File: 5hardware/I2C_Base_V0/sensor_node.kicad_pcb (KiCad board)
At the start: 2 copper layers, 70 parts, among them J1 USB_C_Receptacle_USB2.0, J2 PJ-320D-A, J3 Conn_02x06_Top_Bottom, J4 Conn_01x19_Socket, J5 Conn_01x19_Socket, J6 Conn_01x06_Socket, J7 Conn_01x04_Pin, J8 Conn_01x04_Pin, P1 S3B-PH-SM4-TB, P2 S4B-PH-SM4-TB, P3 S3B-PH-SM4-TB, Q2 Si2371EDS, Q3 Si2371EDS, SW2 SW_Push, SW3 SW_Push, U1 MCP1700x-330xxTO, U10 ESP-12F, U12 APDS-9960, U14 DS3231M, U3 CR2450, U4 CH32V003F4P6, U5 SHT31-DIS, U6 DS1307Z+, U7 XC6206PxxxMR, U8 TPL5110, U9 BH1750FVI-TR, Y1 Crystal, Y2 Crystal

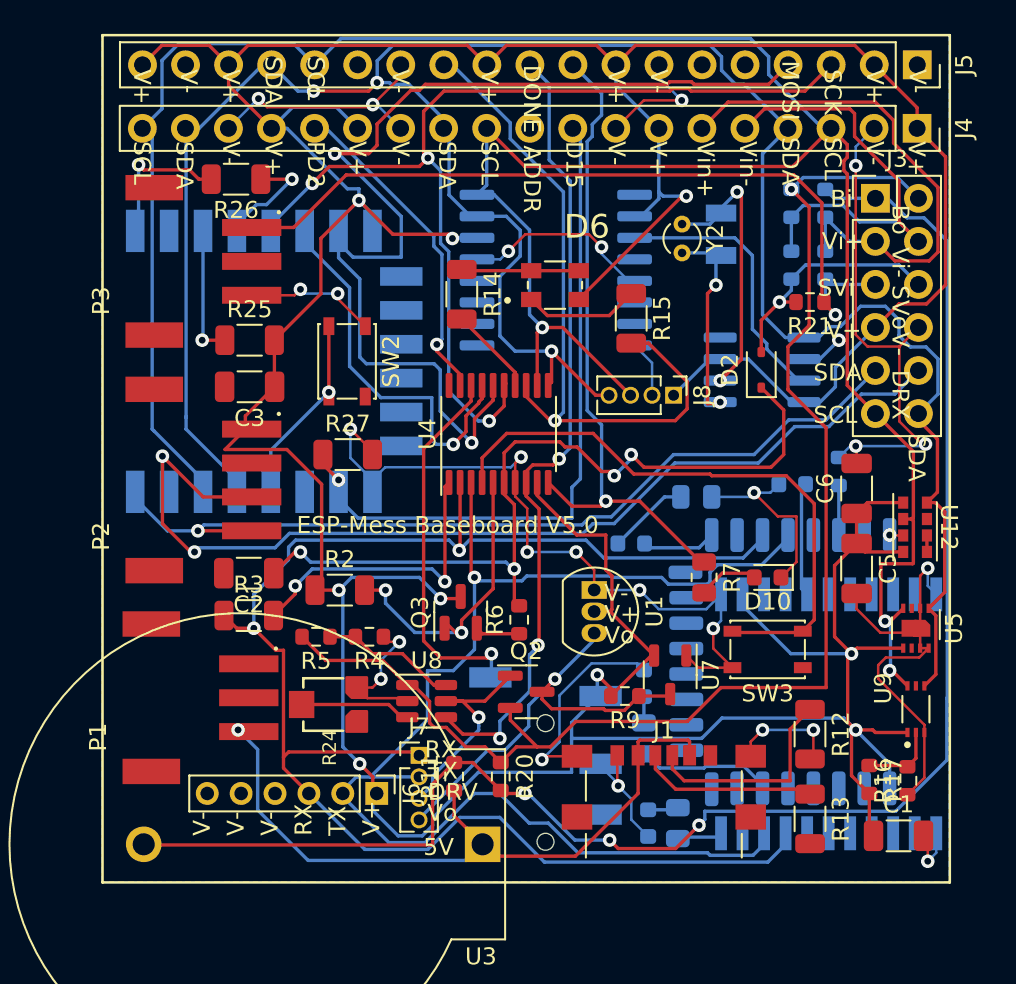
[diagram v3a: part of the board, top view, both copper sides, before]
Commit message: update schematic.
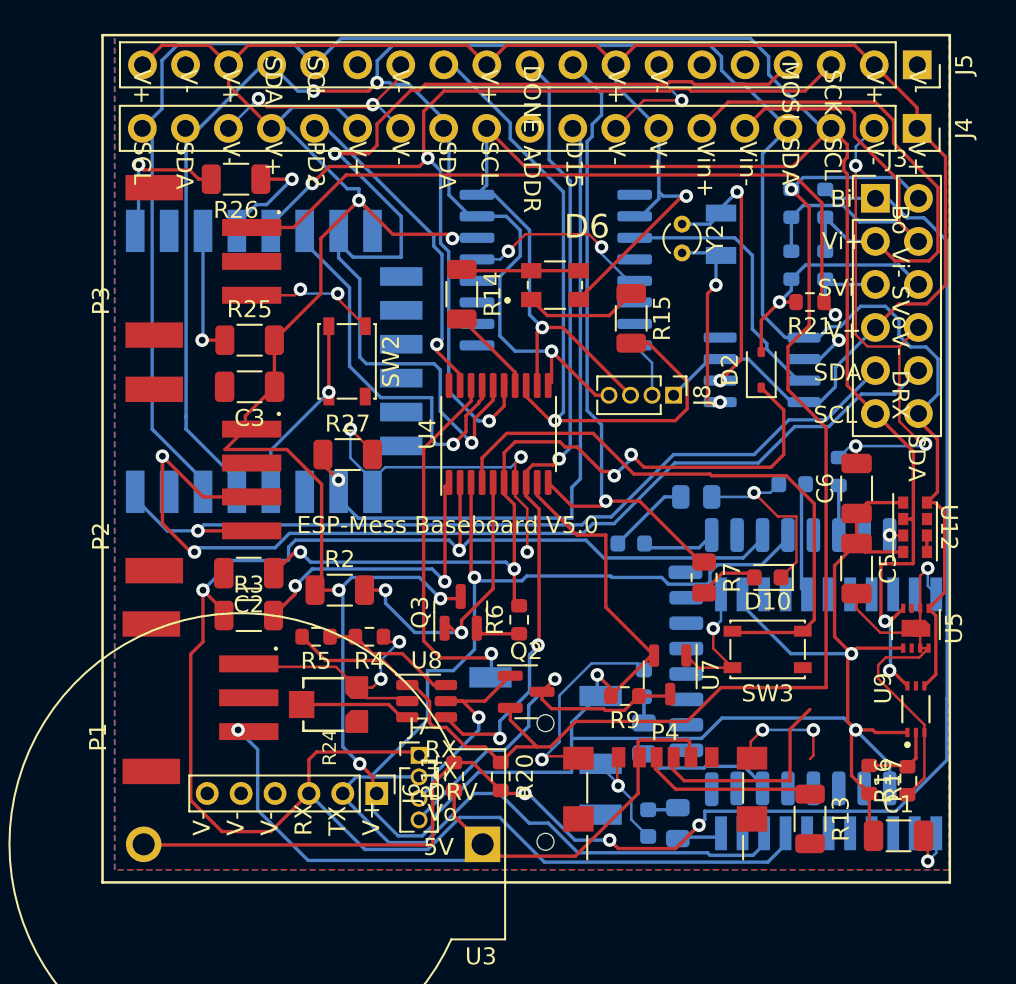
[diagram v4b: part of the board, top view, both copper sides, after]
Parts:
- removed J1: USB_C_Receptacle_USB2.0, Connector_USB:USB_C_Receptacle_GCT_USB4135-GF-A_6P_TopMnt_Horizontal
- removed R12: R, Resistor_SMD:R_1206_3216Metric
- removed U1: MCP1700x-330xxTO, Package_TO_SOT_THT:TO-92_Inline
- added P4: USB_C_Plug_USB2.0, Connector_USB:USB_C_Receptacle_GCT_USB4135-GF-A_6P_TopMnt_Horizontal, F.Cu at (133.3, 91.4)
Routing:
- net unconnected-(P4-VCONN-PadB5): track 0.00 -> 12.7 mm
- net Net-(J1-CC2): track 12.7 -> 0.00 mm
- net RX: track 93.6 -> 105.0 mm
- net GND: track 194.8 -> 187.9 mm, vias 26 -> 24
- net Vo: track 26.0 -> 22.0 mm
- net VCC: track 291.2 -> 290.2 mm

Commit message: update pcb.
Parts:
- removed P4: USB_C_Plug_USB2.0, Connector_USB:USB_C_Receptacle_GCT_USB4135-GF-A_6P_TopMnt_Horizontal
- removed R13: R, Resistor_SMD:R_1206_3216Metric
- moved R8 7.28 mm to (131.4, 80.0)
- moved D1 6.17 mm to (128.4, 79.0), turned to 0 degrees
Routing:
- net +5V: track 42.2 -> 25.3 mm
- net unconnected-(P4-VCONN-PadB5): track 12.7 -> 0.00 mm
- net Net-(P4-CC): track 10.8 -> 0.00 mm
- net Net-(U11-STAT): track 7.88 -> 16.1 mm
- net Bat-Vo: track 79.1 -> 85.5 mm
- net VCC: track 290.2 -> 292.6 mm, vias 9 -> 10
- net Net-(D1-A): track 1.64 -> 2.25 mm
- net GND: track 187.9 -> 187.8 mm, vias 24 -> 21

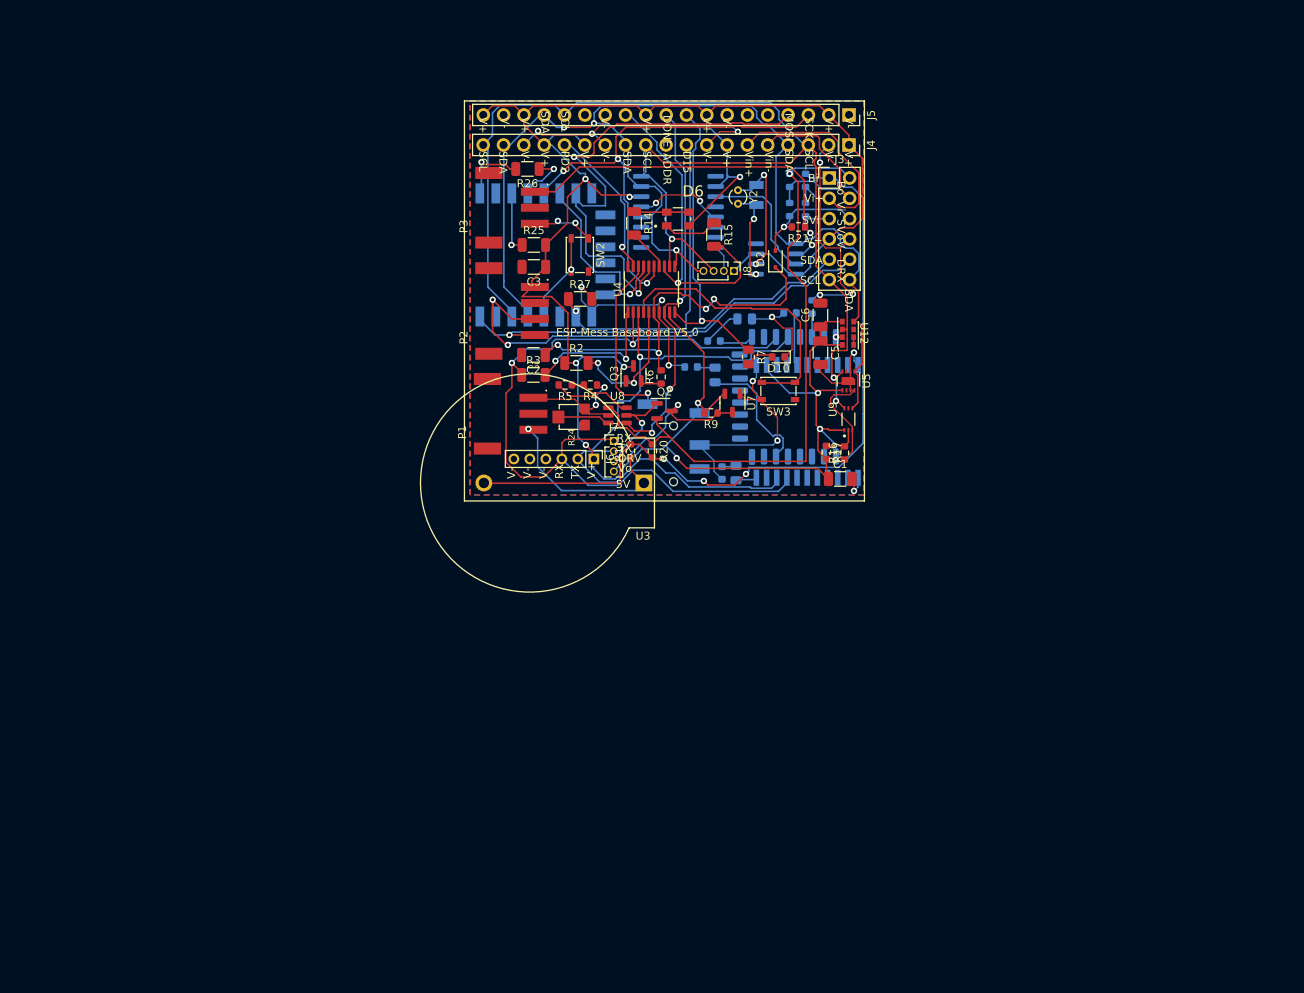
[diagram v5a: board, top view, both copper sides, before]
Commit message: panelized PCBs.
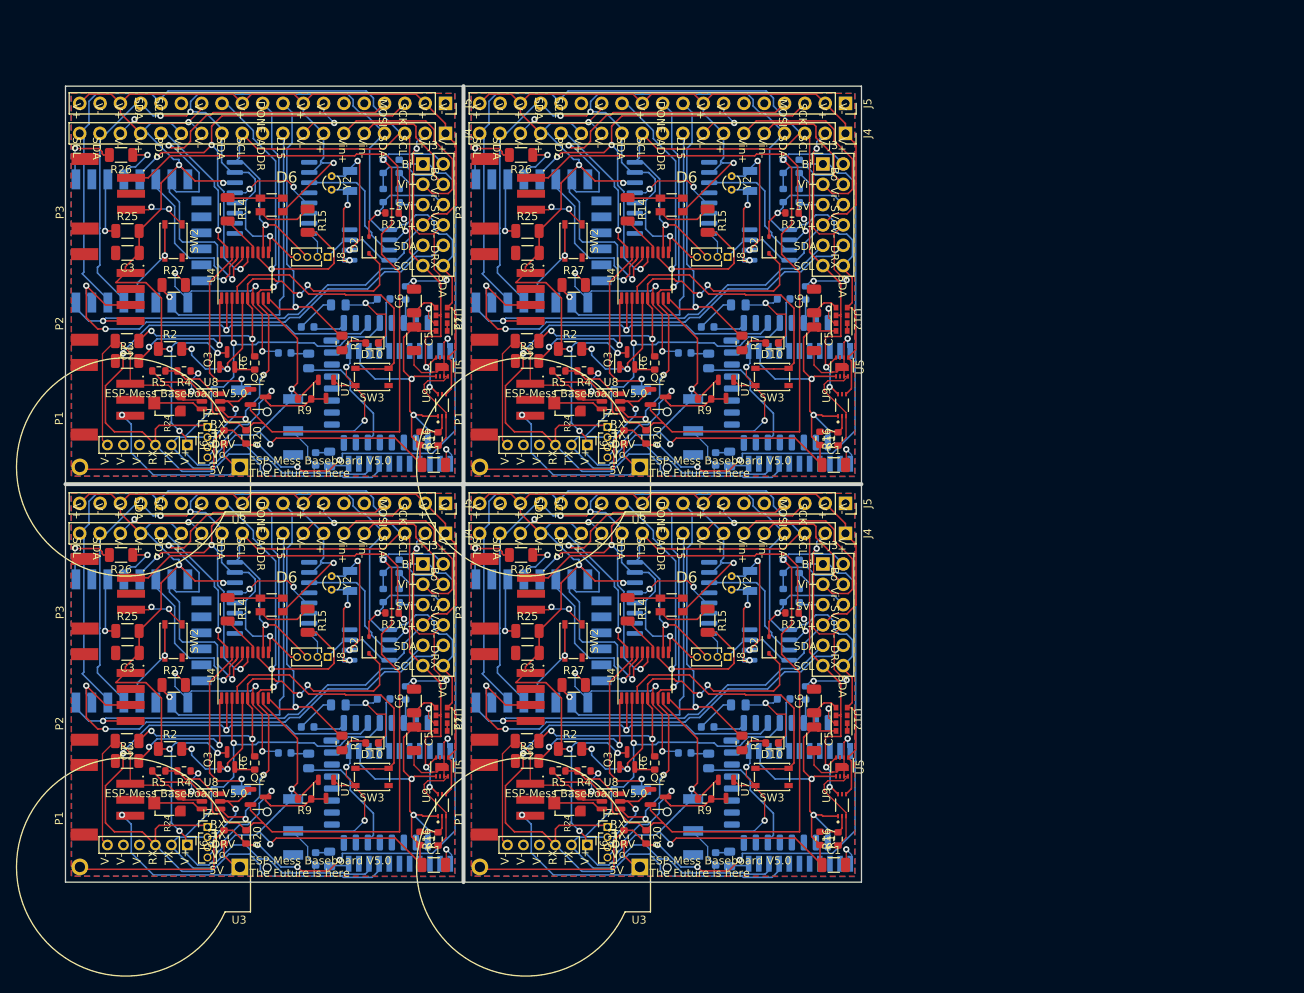
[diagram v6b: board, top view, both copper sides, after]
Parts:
- added C1: C, Capacitor_SMD:C_1206_3216Metric, F.Cu at (146.2, 141.2)
- added C1: C, Capacitor_SMD:C_1206_3216Metric, F.Cu at (96.2, 141.2)
- added C1: C, Capacitor_SMD:C_1206_3216Metric, F.Cu at (96.2, 91.2)
- added C2: C, Capacitor_SMD:C_1206_3216Metric, F.Cu at (57.9, 75.8)
- added C2: C, Capacitor_SMD:C_1206_3216Metric, F.Cu at (57.9, 125.8)
- added C2: C, Capacitor_SMD:C_1206_3216Metric, F.Cu at (107.9, 125.8)
- added C3: C, Capacitor_SMD:C_1206_3216Metric, F.Cu at (58.0, 64.8)
- added C3: C, Capacitor_SMD:C_1206_3216Metric, F.Cu at (58.0, 114.8)
- added C3: C, Capacitor_SMD:C_1206_3216Metric, F.Cu at (108.0, 114.8)
- added C5: C, Capacitor_SMD:C_1206_3216Metric, F.Cu at (143.8, 125.5)
- added C5: C, Capacitor_SMD:C_1206_3216Metric, F.Cu at (93.8, 75.5)
- added C5: C, Capacitor_SMD:C_1206_3216Metric, F.Cu at (93.8, 125.5)
- added C6: C, Capacitor_SMD:C_1206_3216Metric, F.Cu at (93.8, 120.8)
- added C6: C, Capacitor_SMD:C_1206_3216Metric, F.Cu at (93.8, 70.8)
- added C6: C, Capacitor_SMD:C_1206_3216Metric, F.Cu at (143.8, 120.8)
- added D1: LED, LED_SMD:LED_0603_1608Metric, B.Cu at (127.6, 127.2)
- added D1: LED, LED_SMD:LED_0603_1608Metric, B.Cu at (77.6, 77.2)
- added D1: LED, LED_SMD:LED_0603_1608Metric, B.Cu at (77.6, 127.2)
- added D10: LED, LED_SMD:LED_0603_1608Metric, F.Cu at (88.5, 126.0)
- added D10: LED, LED_SMD:LED_0603_1608Metric, F.Cu at (138.5, 126.0)
- added D10: LED, LED_SMD:LED_0603_1608Metric, F.Cu at (88.5, 76.0)
- added D2: D_Schottky, Diode_SMD:D_SOD-323, F.Cu at (88.1, 113.8)
- added D2: D_Schottky, Diode_SMD:D_SOD-323, F.Cu at (88.1, 63.8)
- added D2: D_Schottky, Diode_SMD:D_SOD-323, F.Cu at (138.1, 113.8)
- added D3: LED, LED_SMD:LED_0603_1608Metric, B.Cu at (130.5, 124.0)
- added D3: LED, LED_SMD:LED_0603_1608Metric, B.Cu at (80.5, 124.0)
- added D3: LED, LED_SMD:LED_0603_1608Metric, B.Cu at (80.5, 74.0)
- added D4: LED, LED_SMD:LED_0603_1608Metric, B.Cu at (140.0, 120.5)
- added D4: LED, LED_SMD:LED_0603_1608Metric, B.Cu at (90.0, 120.5)
- added D4: LED, LED_SMD:LED_0603_1608Metric, B.Cu at (90.0, 70.5)
- added D5: LED, LED_SMD:LED_0603_1608Metric, B.Cu at (81.5, 90.5)
- added D5: LED, LED_SMD:LED_0603_1608Metric, B.Cu at (131.5, 140.5)
- added D5: LED, LED_SMD:LED_0603_1608Metric, B.Cu at (81.5, 140.5)
- added D6: LL-R3528RGBC-008-B, R3528RGB:LED_LL-R3528RGBC-008-B, F.Cu at (76.0, 108.8)
- added D6: LL-R3528RGBC-008-B, R3528RGB:LED_LL-R3528RGBC-008-B, F.Cu at (126.0, 108.8)
- added D6: LL-R3528RGBC-008-B, R3528RGB:LED_LL-R3528RGBC-008-B, F.Cu at (76.0, 58.8)
- added J2: PJ-320D-A, A_SensorNode:PJ-320D, B.Cu at (75.4, 87.7)
- added J2: PJ-320D-A, A_SensorNode:PJ-320D, B.Cu at (125.4, 137.7)
- added J2: PJ-320D-A, A_SensorNode:PJ-320D, B.Cu at (75.4, 137.7)
- added J3: Conn_02x06_Top_Bottom, Connector_PinHeader_2.54mm:PinHeader_2x06_P2.54mm_Vertical, F.Cu at (94.9, 53.6)
- added J3: Conn_02x06_Top_Bottom, Connector_PinHeader_2.54mm:PinHeader_2x06_P2.54mm_Vertical, F.Cu at (94.9, 103.6)
- added J3: Conn_02x06_Top_Bottom, Connector_PinHeader_2.54mm:PinHeader_2x06_P2.54mm_Vertical, F.Cu at (144.9, 103.6)
- added J4: Conn_01x19_Socket, Connector_PinSocket_2.54mm:PinSocket_1x19_P2.54mm_Vertical, F.Cu at (97.7, 99.8)
- added J4: Conn_01x19_Socket, Connector_PinSocket_2.54mm:PinSocket_1x19_P2.54mm_Vertical, F.Cu at (97.7, 49.8)
- added J4: Conn_01x19_Socket, Connector_PinSocket_2.54mm:PinSocket_1x19_P2.54mm_Vertical, F.Cu at (147.7, 99.8)
- added J5: Conn_01x19_Socket, Connector_PinSocket_2.54mm:PinSocket_1x19_P2.54mm_Vertical, F.Cu at (97.7, 46.0)
- added J5: Conn_01x19_Socket, Connector_PinSocket_2.54mm:PinSocket_1x19_P2.54mm_Vertical, F.Cu at (147.7, 96.0)
- added J5: Conn_01x19_Socket, Connector_PinSocket_2.54mm:PinSocket_1x19_P2.54mm_Vertical, F.Cu at (97.7, 96.0)
- added J6: Conn_01x06_Socket, Connector_PinHeader_2.00mm:PinHeader_1x06_P2.00mm_Vertical, F.Cu at (65.5, 138.8)
- added J6: Conn_01x06_Socket, Connector_PinHeader_2.00mm:PinHeader_1x06_P2.00mm_Vertical, F.Cu at (65.5, 88.8)
- added J6: Conn_01x06_Socket, Connector_PinHeader_2.00mm:PinHeader_1x06_P2.00mm_Vertical, F.Cu at (115.5, 138.8)
- added J7: Conn_01x04_Pin, Connector_PinHeader_1.27mm:PinHeader_1x04_P1.27mm_Vertical, F.Cu at (68.0, 136.5)
- added J7: Conn_01x04_Pin, Connector_PinHeader_1.27mm:PinHeader_1x04_P1.27mm_Vertical, F.Cu at (68.0, 86.5)
- added J7: Conn_01x04_Pin, Connector_PinHeader_1.27mm:PinHeader_1x04_P1.27mm_Vertical, F.Cu at (118.0, 136.5)
- added J8: Conn_01x04_Pin, Connector_PinHeader_1.27mm:PinHeader_1x04_P1.27mm_Vertical, F.Cu at (83.0, 115.2)
- added J8: Conn_01x04_Pin, Connector_PinHeader_1.27mm:PinHeader_1x04_P1.27mm_Vertical, F.Cu at (83.0, 65.2)
- added J8: Conn_01x04_Pin, Connector_PinHeader_1.27mm:PinHeader_1x04_P1.27mm_Vertical, F.Cu at (133.0, 115.2)
- added P1: S3B-PH-SM4-TB, S3B-PH:JST_S3B-PH-SM4-TB, F.Cu at (58.3, 133.1)
- added P1: S3B-PH-SM4-TB, S3B-PH:JST_S3B-PH-SM4-TB, F.Cu at (108.3, 133.1)
- added P1: S3B-PH-SM4-TB, S3B-PH:JST_S3B-PH-SM4-TB, F.Cu at (58.3, 83.1)
- added P2: S4B-PH-SM4-TB, S4B-PH:JST_S4B-PH-SM4-TB, F.Cu at (58.4, 70.2)
- added P2: S4B-PH-SM4-TB, S4B-PH:JST_S4B-PH-SM4-TB, F.Cu at (108.3, 120.2)
- added P2: S4B-PH-SM4-TB, S4B-PH:JST_S4B-PH-SM4-TB, F.Cu at (58.4, 120.2)
- added P3: S3B-PH-SM4-TB, S3B-PH:JST_S3B-PH-SM4-TB, F.Cu at (108.4, 107.3)
- added P3: S3B-PH-SM4-TB, S3B-PH:JST_S3B-PH-SM4-TB, F.Cu at (58.4, 57.4)
- added P3: S3B-PH-SM4-TB, S3B-PH:JST_S3B-PH-SM4-TB, F.Cu at (58.4, 107.3)
- added Q2: Si2371EDS, Package_TO_SOT_SMD:SOT-23, F.Cu at (74.3, 132.8)
- added Q2: Si2371EDS, Package_TO_SOT_SMD:SOT-23, F.Cu at (124.3, 132.8)
- added Q2: Si2371EDS, Package_TO_SOT_SMD:SOT-23, F.Cu at (74.3, 82.8)
- added Q3: Si2371EDS, Package_TO_SOT_SMD:SOT-23, F.Cu at (70.4, 128.1)
- added Q3: Si2371EDS, Package_TO_SOT_SMD:SOT-23, F.Cu at (70.4, 78.1)
- added Q3: Si2371EDS, Package_TO_SOT_SMD:SOT-23, F.Cu at (120.4, 128.1)
- added R1: R, Resistor_SMD:R_0603_1608Metric, B.Cu at (142.7, 119.8)
- added R1: R, Resistor_SMD:R_0603_1608Metric, B.Cu at (92.7, 119.8)
- added R1: R, Resistor_SMD:R_0603_1608Metric, B.Cu at (92.7, 69.8)
- added R10: R, Resistor_SMD:R_0805_2012Metric, B.Cu at (133.2, 140.5)
- added R10: R, Resistor_SMD:R_0805_2012Metric, B.Cu at (83.2, 90.5)
- added R10: R, Resistor_SMD:R_0805_2012Metric, B.Cu at (83.2, 140.5)
- added R11: R, Resistor_SMD:R_0603_1608Metric, F.Cu at (70.0, 87.8)
- added R11: R, Resistor_SMD:R_0603_1608Metric, F.Cu at (120.0, 137.8)
- added R11: R, Resistor_SMD:R_0603_1608Metric, F.Cu at (70.0, 137.8)
- added R14: R, Resistor_SMD:R_1206_3216Metric, F.Cu at (70.5, 59.3)
- added R14: R, Resistor_SMD:R_1206_3216Metric, F.Cu at (70.5, 109.3)
- added R14: R, Resistor_SMD:R_1206_3216Metric, F.Cu at (120.5, 109.3)
- added R15: R, Resistor_SMD:R_1206_3216Metric, F.Cu at (80.5, 60.7)
- added R15: R, Resistor_SMD:R_1206_3216Metric, F.Cu at (80.5, 110.7)
- added R15: R, Resistor_SMD:R_1206_3216Metric, F.Cu at (130.5, 110.7)
- added R16: R, Resistor_SMD:R_0603_1608Metric, F.Cu at (96.8, 138.0)
- added R16: R, Resistor_SMD:R_0603_1608Metric, F.Cu at (96.8, 88.0)
- added R16: R, Resistor_SMD:R_0603_1608Metric, F.Cu at (146.8, 138.0)
- added R17: R, Resistor_SMD:R_0603_1608Metric, F.Cu at (144.5, 137.9)
- added R17: R, Resistor_SMD:R_0603_1608Metric, F.Cu at (94.5, 87.9)
- added R17: R, Resistor_SMD:R_0603_1608Metric, F.Cu at (94.5, 137.9)
- added R18: R, Resistor_SMD:R_0603_1608Metric, B.Cu at (91.9, 103.9)
- added R18: R, Resistor_SMD:R_0603_1608Metric, B.Cu at (91.9, 53.9)
- added R18: R, Resistor_SMD:R_0603_1608Metric, B.Cu at (141.9, 103.9)
- added R19: R, Resistor_SMD:R_0603_1608Metric, B.Cu at (139.9, 103.9)
- added R19: R, Resistor_SMD:R_0603_1608Metric, B.Cu at (89.9, 53.9)
- added R19: R, Resistor_SMD:R_0603_1608Metric, B.Cu at (89.9, 103.9)
- added R2: R, Resistor_SMD:R_1206_3216Metric, F.Cu at (113.3, 126.8)
- added R2: R, Resistor_SMD:R_1206_3216Metric, F.Cu at (63.3, 76.8)
- added R2: R, Resistor_SMD:R_1206_3216Metric, F.Cu at (63.3, 126.8)
- added R20: R, Resistor_SMD:R_0603_1608Metric, F.Cu at (72.8, 87.8)
- added R20: R, Resistor_SMD:R_0603_1608Metric, F.Cu at (72.8, 137.8)
- added R20: R, Resistor_SMD:R_0603_1608Metric, F.Cu at (122.8, 137.8)
- added R21: R, Resistor_SMD:R_0603_1608Metric, F.Cu at (141.0, 109.8)
- added R21: R, Resistor_SMD:R_0603_1608Metric, F.Cu at (91.0, 59.8)
- added R21: R, Resistor_SMD:R_0603_1608Metric, F.Cu at (91.0, 109.8)
- added R22: R, Resistor_SMD:R_0603_1608Metric, B.Cu at (91.9, 107.6)
- added R22: R, Resistor_SMD:R_0603_1608Metric, B.Cu at (141.9, 107.6)
- added R22: R, Resistor_SMD:R_0603_1608Metric, B.Cu at (91.9, 57.6)
- added R23: R, Resistor_SMD:R_0603_1608Metric, B.Cu at (89.9, 107.6)
- added R23: R, Resistor_SMD:R_0603_1608Metric, B.Cu at (139.9, 107.6)
- added R23: R, Resistor_SMD:R_0603_1608Metric, B.Cu at (89.9, 57.6)
- added R24: EVM3ESX50B12, EVM3ES:EMV3ESX50B12, F.Cu at (113.0, 133.5)
- added R24: EVM3ESX50B12, EVM3ES:EMV3ESX50B12, F.Cu at (63.0, 133.5)
- added R24: EVM3ESX50B12, EVM3ES:EMV3ESX50B12, F.Cu at (63.0, 83.5)
- added R25: R, Resistor_SMD:R_1206_3216Metric, F.Cu at (108.0, 112.0)
- added R25: R, Resistor_SMD:R_1206_3216Metric, F.Cu at (58.0, 62.0)
- added R25: R, Resistor_SMD:R_1206_3216Metric, F.Cu at (58.0, 112.0)
- added R26: R, Resistor_SMD:R_1206_3216Metric, F.Cu at (57.1, 52.5)
- added R26: R, Resistor_SMD:R_1206_3216Metric, F.Cu at (57.1, 102.5)
- added R26: R, Resistor_SMD:R_1206_3216Metric, F.Cu at (107.1, 102.5)
- added R27: R, Resistor_SMD:R_1206_3216Metric, F.Cu at (63.7, 118.8)
- added R27: R, Resistor_SMD:R_1206_3216Metric, F.Cu at (63.7, 68.8)
- added R27: R, Resistor_SMD:R_1206_3216Metric, F.Cu at (113.7, 118.8)
- added R28: R, Resistor_SMD:R_0805_2012Metric, B.Cu at (134.3, 121.2)
- added R28: R, Resistor_SMD:R_0805_2012Metric, B.Cu at (84.3, 71.2)
- added R28: R, Resistor_SMD:R_0805_2012Metric, B.Cu at (84.3, 121.2)
- added R3: R, Resistor_SMD:R_1206_3216Metric, F.Cu at (57.9, 128.2)
- added R3: R, Resistor_SMD:R_1206_3216Metric, F.Cu at (107.9, 128.2)
- added R3: R, Resistor_SMD:R_1206_3216Metric, F.Cu at (57.9, 78.2)
- added R4: R, Resistor_SMD:R_0603_1608Metric, F.Cu at (65.0, 79.5)
- added R4: R, Resistor_SMD:R_0603_1608Metric, F.Cu at (115.0, 129.5)
- added R4: R, Resistor_SMD:R_0603_1608Metric, F.Cu at (65.0, 129.5)
- added R5: R, Resistor_SMD:R_0603_1608Metric, F.Cu at (61.9, 79.5)
- added R5: R, Resistor_SMD:R_0603_1608Metric, F.Cu at (111.9, 129.5)
- added R5: R, Resistor_SMD:R_0603_1608Metric, F.Cu at (61.9, 129.5)
- added R6: R, Resistor_SMD:R_0603_1608Metric, F.Cu at (123.9, 128.5)
- added R6: R, Resistor_SMD:R_0603_1608Metric, F.Cu at (73.9, 128.5)
- added R6: R, Resistor_SMD:R_0603_1608Metric, F.Cu at (73.9, 78.5)
- added R7: R, Resistor_SMD:R_0805_2012Metric, F.Cu at (84.8, 126.0)
- added R7: R, Resistor_SMD:R_0805_2012Metric, F.Cu at (84.8, 76.0)
- added R7: R, Resistor_SMD:R_0805_2012Metric, F.Cu at (134.8, 126.0)
- added R8: R, Resistor_SMD:R_0805_2012Metric, B.Cu at (130.6, 128.2)
- added R8: R, Resistor_SMD:R_0805_2012Metric, B.Cu at (80.6, 128.2)
- added R8: R, Resistor_SMD:R_0805_2012Metric, B.Cu at (80.6, 78.2)
- added R9: R, Resistor_SMD:R_0603_1608Metric, F.Cu at (80.1, 133.0)
- added R9: R, Resistor_SMD:R_0603_1608Metric, F.Cu at (130.1, 133.0)
- added R9: R, Resistor_SMD:R_0603_1608Metric, F.Cu at (80.1, 83.0)
- added SW2: SW_Push, Button_Switch_SMD:SW_SPST_PTS810, F.Cu at (63.7, 63.2)
- added SW2: SW_Push, Button_Switch_SMD:SW_SPST_PTS810, F.Cu at (113.7, 113.2)
- added SW2: SW_Push, Button_Switch_SMD:SW_SPST_PTS810, F.Cu at (63.7, 113.2)
- added SW3: SW_Push, Button_Switch_SMD:SW_SPST_PTS810, F.Cu at (88.5, 80.2)
- added SW3: SW_Push, Button_Switch_SMD:SW_SPST_PTS810, F.Cu at (88.5, 130.2)
- added SW3: SW_Push, Button_Switch_SMD:SW_SPST_PTS810, F.Cu at (138.5, 130.2)
- added U10: ESP-12F, A_SensorNode:ESP12_SMD, B.Cu at (48.9, 105.2)
- added U10: ESP-12F, A_SensorNode:ESP12_SMD, B.Cu at (48.9, 55.2)
- added U10: ESP-12F, A_SensorNode:ESP12_SMD, B.Cu at (98.9, 105.2)
- added U11: ~, A_SensorNode:JDY-Base, B.Cu at (83.5, 73.5)
- added U11: ~, A_SensorNode:JDY-Base, B.Cu at (83.5, 123.5)
- added U11: ~, A_SensorNode:JDY-Base, B.Cu at (133.5, 123.5)
- added U12: APDS-9960, Sensor:Avago_APDS-9960, F.Cu at (97.2, 123.0)
- added U12: APDS-9960, Sensor:Avago_APDS-9960, F.Cu at (97.2, 73.0)
- added U12: APDS-9960, Sensor:Avago_APDS-9960, F.Cu at (147.2, 123.0)
- added U14: DS3231M, Package_SO:SOIC-16W_7.5x10.3mm_P1.27mm, B.Cu at (76.0, 107.9)
- added U14: DS3231M, Package_SO:SOIC-16W_7.5x10.3mm_P1.27mm, B.Cu at (126.0, 107.9)
- added U14: DS3231M, Package_SO:SOIC-16W_7.5x10.3mm_P1.27mm, B.Cu at (76.0, 57.9)
- added U2: ~, A_SensorNode:E104-BT07, B.Cu at (99.2, 92.3)
- added U2: ~, A_SensorNode:E104-BT07, B.Cu at (99.2, 142.3)
- added U2: ~, A_SensorNode:E104-BT07, B.Cu at (149.2, 142.3)
- added U3: CR2450, Battery:BatteryHolder_ComfortableElectronic_CH273-2450_1x2450, F.Cu at (122.0, 141.5)
- added U3: CR2450, Battery:BatteryHolder_ComfortableElectronic_CH273-2450_1x2450, F.Cu at (72.0, 91.5)
- added U3: CR2450, Battery:BatteryHolder_ComfortableElectronic_CH273-2450_1x2450, F.Cu at (72.0, 141.5)
- added U4: CH32V003F4P6, Package_SO:TSSOP-20_4.4x6.5mm_P0.65mm, F.Cu at (72.6, 67.5)
- added U4: CH32V003F4P6, Package_SO:TSSOP-20_4.4x6.5mm_P0.65mm, F.Cu at (72.6, 117.5)
- added U4: CH32V003F4P6, Package_SO:TSSOP-20_4.4x6.5mm_P0.65mm, F.Cu at (122.6, 117.5)
- added U5: SHT31-DIS, Sensor_Humidity:Sensirion_DFN-8-1EP_2.5x2.5mm_P0.5mm_EP1.1x1.7mm, F.Cu at (97.3, 79.0)
- added U5: SHT31-DIS, Sensor_Humidity:Sensirion_DFN-8-1EP_2.5x2.5mm_P0.5mm_EP1.1x1.7mm, F.Cu at (97.3, 129.0)
- added U5: SHT31-DIS, Sensor_Humidity:Sensirion_DFN-8-1EP_2.5x2.5mm_P0.5mm_EP1.1x1.7mm, F.Cu at (147.3, 129.0)
- added U6: DS1307Z+, Package_SO:SOIC-8_3.9x4.9mm_P1.27mm, B.Cu at (88.2, 63.8)
- added U6: DS1307Z+, Package_SO:SOIC-8_3.9x4.9mm_P1.27mm, B.Cu at (88.2, 113.8)
- added U6: DS1307Z+, Package_SO:SOIC-8_3.9x4.9mm_P1.27mm, B.Cu at (138.2, 113.8)
- added U7: XC6206PxxxMR, Package_TO_SOT_SMD:SOT-23-3, F.Cu at (82.8, 81.8)
- added U7: XC6206PxxxMR, Package_TO_SOT_SMD:SOT-23-3, F.Cu at (82.8, 131.8)
- added U7: XC6206PxxxMR, Package_TO_SOT_SMD:SOT-23-3, F.Cu at (132.8, 131.8)
- added U8: TPL5110, Package_TO_SOT_SMD:SOT-23-6, F.Cu at (68.4, 133.3)
- added U8: TPL5110, Package_TO_SOT_SMD:SOT-23-6, F.Cu at (68.4, 83.3)
- added U8: TPL5110, Package_TO_SOT_SMD:SOT-23-6, F.Cu at (118.4, 133.3)
- added U9: BH1750FVI-TR, BH1750:XDCR_BH1750FVI-TR, F.Cu at (147.3, 133.8)
- added U9: BH1750FVI-TR, BH1750:XDCR_BH1750FVI-TR, F.Cu at (97.3, 133.8)
- added U9: BH1750FVI-TR, BH1750:XDCR_BH1750FVI-TR, F.Cu at (97.3, 83.8)
- added Y1: Crystal, Crystal:Crystal_SMD_3215-2Pin_3.2x1.5mm, B.Cu at (135.8, 105.8)
- added Y1: Crystal, Crystal:Crystal_SMD_3215-2Pin_3.2x1.5mm, B.Cu at (85.8, 105.8)
- added Y1: Crystal, Crystal:Crystal_SMD_3215-2Pin_3.2x1.5mm, B.Cu at (85.8, 55.8)
- added Y2: Crystal, Crystal:Crystal_Round_D1.5mm_Vertical, F.Cu at (133.5, 105.2)
- added Y2: Crystal, Crystal:Crystal_Round_D1.5mm_Vertical, F.Cu at (83.5, 105.2)
- added Y2: Crystal, Crystal:Crystal_Round_D1.5mm_Vertical, F.Cu at (83.5, 55.1)
- moved U3 2.06 mm to (122.0, 91.5)
- moved U11 2.03 mm to (133.5, 73.5)
- moved U2 2.00 mm to (149.2, 92.3)
- moved C5 1.92 mm to (143.8, 75.5)
- moved C6 1.92 mm to (143.8, 70.8)
- moved D1 1.92 mm to (127.6, 77.2)
- moved D10 1.92 mm to (138.5, 76.0)
- moved D2 1.92 mm to (138.1, 63.8)
- moved D3 1.92 mm to (130.5, 74.0)
- moved D4 1.92 mm to (140.0, 70.5)
- moved D5 1.92 mm to (131.5, 90.5)
- moved J2 1.92 mm to (125.4, 87.7)
- moved J8 1.92 mm to (133.0, 65.2)
- moved R1 1.92 mm to (142.7, 69.8)
- moved R10 1.92 mm to (133.2, 90.5)
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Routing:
- net VCC: track 292.6 -> 1176.6 mm, vias 10 -> 40
- net GND: track 187.8 -> 846.6 mm, vias 21 -> 84
- net SCL (5): track 160.1 -> 639.4 mm, vias 4 -> 16
- net SDA (4): track 142.8 -> 571.9 mm, vias 3 -> 12
- net RX: track 105.0 -> 393.2 mm, vias 2 -> 8
- net Bat-Vi: track 95.1 -> 380.1 mm, vias 3 -> 12
- net Bat-Vo: track 85.5 -> 330.9 mm, vias 1 -> 4
- net TX: track 76.2 -> 303.7 mm, vias 1 -> 4
- net MOSI: track 63.0 -> 252.4 mm, vias 2 -> 8
- net D3_RX: track 61.2 -> 243.9 mm, vias 2 -> 8
- net SCK: track 60.2 -> 238.8 mm, vias 3 -> 12
- net D1_TX: track 52.3 -> 209.1 mm, vias 1 -> 4
- net Solar_Vi: track 48.4 -> 192.9 mm, vias 1 -> 4
- net Net-(D2-K): track 47.9 -> 191.6 mm, vias 4 -> 16
- net DONE: track 48.0 -> 190.1 mm, vias 3 -> 12
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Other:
- board outline added: 99.5 x 99.5 mm
- board text added: "The Future is here"
- board text added: "V-CUT"
